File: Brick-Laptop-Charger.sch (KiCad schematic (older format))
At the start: 46 parts, among them P1 TST, P10 Power Out, P2 TST, P3 TST, P4 TST, P5 TST, P6 TST, P7 TST, P8 Battery 1, P9 Battery 2, Q1 MOS_N, Q2 MOS_N, U1 LM5117*PM*

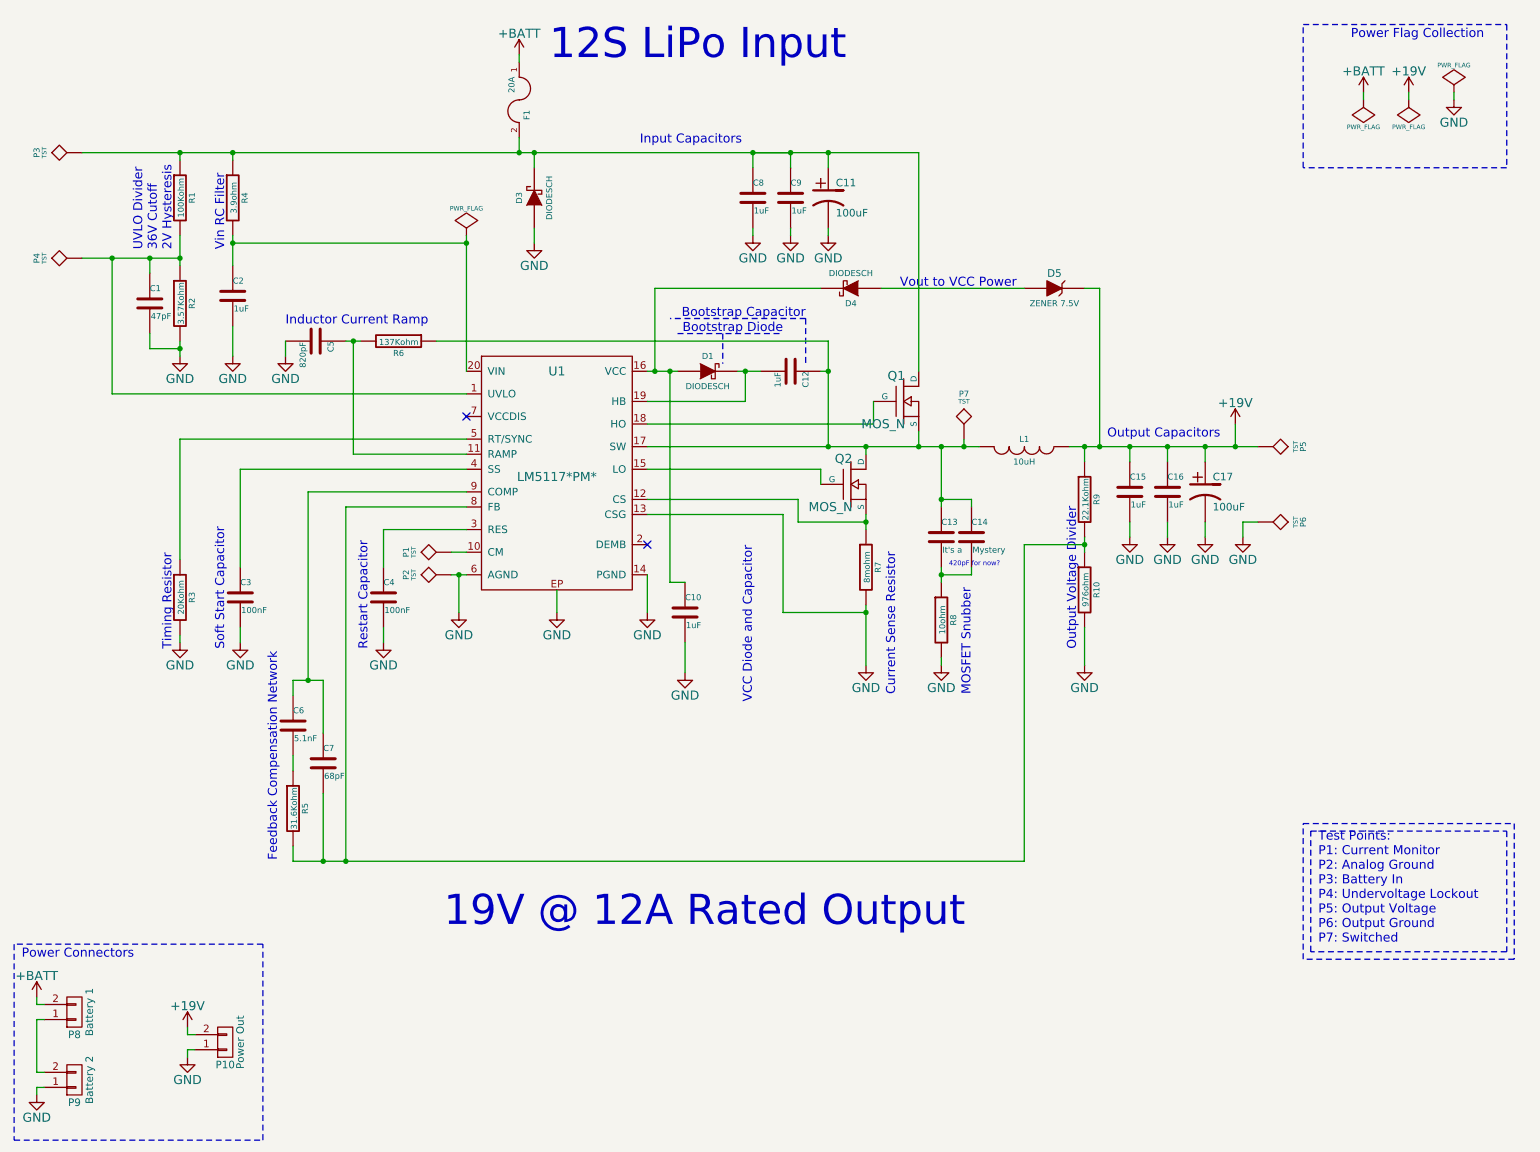
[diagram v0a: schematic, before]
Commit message: Separated analog and power grounds.  Most of power current now flows through a separate path from analog circuitry (see exposed trace on bottom of PCB).  Reduced capacitive coupling between ground planes and MOSFET switches.  Smoothed copper pours.  Added power in LED.
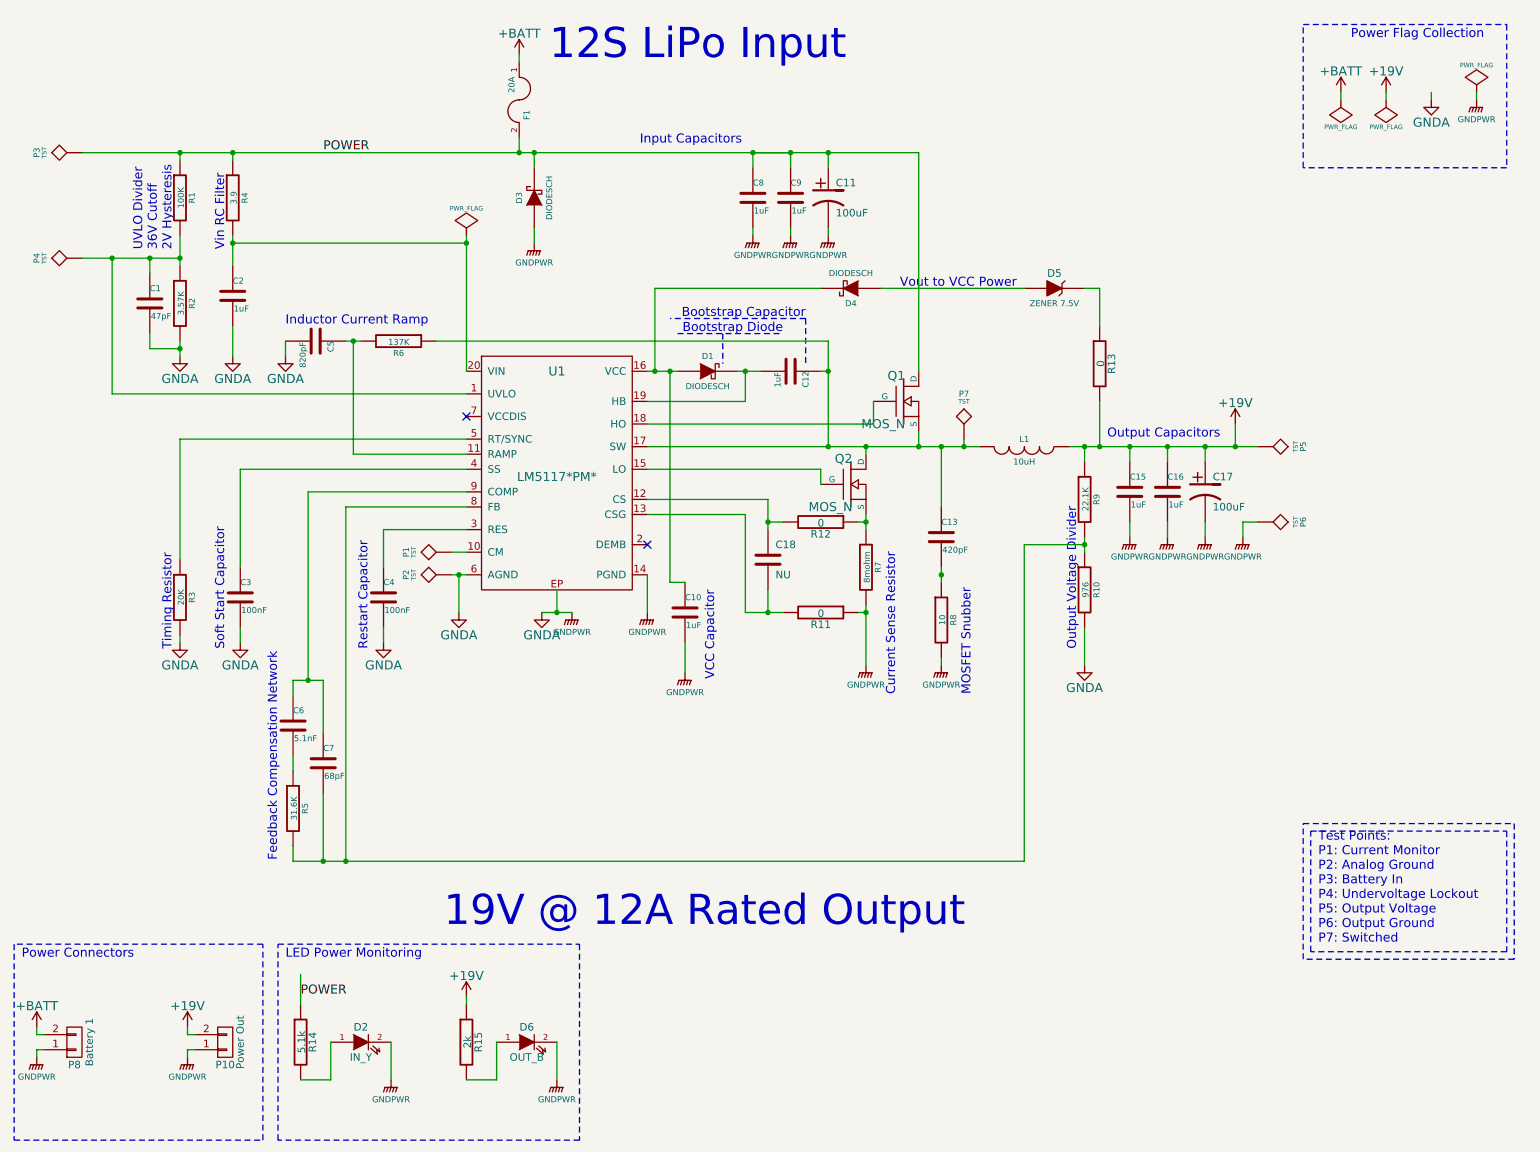
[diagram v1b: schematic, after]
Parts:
- removed C14: Mystery, Discret:C1, symbol C
- removed P9: Battery 2, This:BIG_CONN, symbol CONN_01X02
- added C18: NU, Capacitors_SMD:C_0805, symbol C
- added D2: IN_Y, LEDs:LED-0805, symbol LED
- added D6: OUT_B, LEDs:LED-0805, symbol LED
- added R11, R12, R13: 0, Resistors_SMD:R_0805, symbol R
- added R14: 5.1k, Resistors_SMD:R_0805, symbol R
- added R15: 2k, Resistors_SMD:R_0805, symbol R
- C13: value It's a -> 420pF
- R1: value 100Kohm -> 100K
- R10: value 976ohm -> 976
- R2: value 3.57Kohm -> 3.57K
- R3: value 20Kohm -> 20K
- R4: value 3.9ohm -> 3.9
- R5: value 31.6Kohm -> 31.6K
- R6: value 137Kohm -> 137K
- R8: value 10ohm -> 10
- R9: value 22.1Kohm -> 22.1K
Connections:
- net +19V: now also R13.2, R15.1; no longer D5.2 (K)
- net at Q2.S, R7.1: now also R12.1; no longer U1.12 (CS)
- net POWER: now reaches C11.1, C8.1, C9.1, D3.2 (K), F1.2, P3.1, Q1.D, R1.1, R4.1
- net POWER: now also R14.1
- net GNDA: now reaches P8.1 (P1)
- net GNDA: now also C1.2, C10.2, C11.2, C15.2, C16.2, C17.2, C2.2, C3.2, C4.2, C5.2, C8.2, C9.2, D3.1 (A), P10.1 (P1), P2.1, P6.1, R10.2, R2.2, R3.2, R7.2, R8.2, U1.14 (PGND), U1.6 (AGND), U1.EP, D2.2 (K), D6.2 (K), R11.1
- removed net GND: C1.2, C10.2, C11.2, C15.2, C16.2, C17.2, C2.2, C3.2, C4.2, C5.2, C8.2, C9.2, D3.1 (A), P10.1 (P1), P2.1, P6.1, R10.2, R2.2, R3.2, R7.2, R8.2, U1.13 (CSG), U1.14 (PGND), U1.6 (AGND), U1.EP
- new net: C18.1, R12.2, U1.12 (CS)
- new net: C18.2, R11.2, U1.13 (CSG)
- new net: D5.2 (K), R13.1
- new net: D2.1 (A), R14.2
- new net: D6.1 (A), R15.2
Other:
- note added: "LED Power Monitoring"
- note added: "VCC Capacitor"
- note removed: "420pF for now?"
- note removed: "VCC Diode and Capacitor"
- moved on the sheet: P8

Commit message: Moved files, removed backup files, added important notes about inductor selection, added images
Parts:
- removed D2: IN_Y, LEDs:LED-0805, symbol LED
- removed R14: 5.1k, Resistors_SMD:R_0805, symbol R
- C1, C10, C12, C13, C15, C16, C18, C2, C3, C4, C5, C6, C7, C8, C9: symbol C -> C-RESCUE-Brick-Laptop-Charger
- C11, C17: symbol CP1 -> CP1-RESCUE-Brick-Laptop-Charger
- D5: symbol ZENER -> ZENER-RESCUE-Brick-Laptop-Charger
- D6: symbol LED -> LED-RESCUE-Brick-Laptop-Charger
- R1, R10, R11, R12, R13, R15, R2, R3, R4, R5, R6, R7, R8, R9: symbol R -> R-RESCUE-Brick-Laptop-Charger
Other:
- moved on the sheet: D6, R15
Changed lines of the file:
@@
 EESchema Schematic File Version 2
+LIBS:Brick-Laptop-Charger-rescue
 LIBS:+19v
 LIBS:power
@@
 LIBS:memory
 LIBS:xilinx
-LIBS:special
 LIBS:microcontrollers
 LIBS:dsp
@@
 Sheet 1 1
 Title "Yellow Brick Laptop Charger Schematic"
-Date "Tue 10 Feb 2015"
-Rev "C"
+Date "2015-08-12"
+Rev "D"
 Comp "IEEE UCR, UCR UAS"
 Comment1 "By: Brandon (blu006@ucr.edu)"
@@
 $EndComp
 $Comp
-L C C15
+L C-RESCUE-Brick-Laptop-Charger C15
 U 1 1 54992FF6
 P 7950 3650
@@
 $EndComp
 $Comp
-L C C16
+L C-RESCUE-Brick-Laptop-Charger C16
 U 1 1 54993133
 P 8200 3650
@@
 $EndComp
 $Comp
-L CP1 C17
+L CP1-RESCUE-Brick-Laptop-Charger C17
 U 1 1 54993168
 P 8450 3650
@@
 $EndComp
 $Comp
-L C C12
+L C-RESCUE-Brick-Laptop-Charger C12
 U 1 1 54993759
 P 5700 2850
@@
 $EndComp
 $Comp
-L C C10
+L C-RESCUE-Brick-Laptop-Charger C10
 U 1 1 54993858
 P 5000 4450
@@
 $EndComp
 $Comp
-L R R8
+L R-RESCUE-Brick-Laptop-Charger R8
 U 1 1 54993C5B
 P 6700 4500
@@
 $EndComp
 $Comp
-L R R7
+L R-RESCUE-Brick-Laptop-Charger R7
 U 1 1 54993FF3
 P 6200 4150
@@
 $EndComp
 $Comp
-L C C5
+L C-RESCUE-Brick-Laptop-Charger C5
 U 1 1 54995580
 P 2550 2650
@@
 $EndComp
 $Comp
-L R R6
+L R-RESCUE-Brick-Laptop-Charger R6
 U 1 1 549959D5
 P 3100 2650
@@
 $EndComp
 $Comp
-L R R3
+L R-RESCUE-Brick-Laptop-Charger R3
 U 1 1 54996578
 P 1650 4350
@@
 $EndComp
 $Comp
-L R R1
+L R-RESCUE-Brick-Laptop-Charger R1
 U 1 1 5499683E
 P 1650 1700
@@
 $EndComp
 $Comp
-L R R2
+L R-RESCUE-Brick-Laptop-Charger R2
 U 1 1 549969E4
 P 1650 2400
@@
 $EndComp
 $Comp
-L R R4
+L R-RESCUE-Brick-Laptop-Charger R4
 U 1 1 54996D8E
 P 2000 1700
@@
 $EndComp
 $Comp
-L C C2
+L C-RESCUE-Brick-Laptop-Charger C2
 U 1 1 54996DF9
 P 2000 2350
@@
 $EndComp
 $Comp
-L C C1
+L C-RESCUE-Brick-Laptop-Charger C1
 U 1 1 54997D5E
 P 1450 2400
@@
 $EndComp
 $Comp
-L C C3
+L C-RESCUE-Brick-Laptop-Charger C3
 U 1 1 54998944
 P 2050 4350
@@
 Current Sense Resistor
 $Comp
-L C C4
+L C-RESCUE-Brick-Laptop-Charger C4
 U 1 1 54999F5C
 P 3000 4350
@@
 $EndComp
 $Comp
-L R R9
+L R-RESCUE-Brick-Laptop-Charger R9
 U 1 1 5499B371
 P 7650 3700
@@
 $EndComp
 $Comp
-L R R10
+L R-RESCUE-Brick-Laptop-Charger R10
 U 1 1 5499B44E
 P 7650 4300
@@
 Output Voltage Divider
 $Comp
-L C C7
+L C-RESCUE-Brick-Laptop-Charger C7
 U 1 1 5499CDE4
 P 2600 5450
@@
 $EndComp
 $Comp
-L C C6
+L C-RESCUE-Brick-Laptop-Charger C6
 U 1 1 5499CE97
 P 2400 5200
@@
 $EndComp
 $Comp
-L R R5
+L R-RESCUE-Brick-Laptop-Charger R5
 U 1 1 5499CEEA
 P 2400 5750
@@
 VCC Capacitor
 $Comp
-L C C8
+L C-RESCUE-Brick-Laptop-Charger C8
 U 1 1 549A0DE6
 P 5450 1700
@@
 $EndComp
 $Comp
-L C C9
+L C-RESCUE-Brick-Laptop-Charger C9
 U 1 1 549A0DEC
 P 5700 1700
@@
 $EndComp
 $Comp
-L CP1 C11
+L CP1-RESCUE-Brick-Laptop-Charger C11
 U 1 1 549A0DF2
 P 5950 1700
@@
 Wire Wire Line
 	1000 1400 6550 1400
-Connection ~ 6700 4200
 Wire Wire Line
 	2400 6000 2400 6100
@@
 	4000 2000 4000 1900
 $Comp
-L ZENER D5
+L ZENER-RESCUE-Brick-Laptop-Charger D5
 U 1 1 549C5A81
 P 7450 2300
@@
 	700  7350 700  7400
 $Comp
-L R R11
+L R-RESCUE-Brick-Laptop-Charger R11
 U 1 1 54D43E7E
 P 5900 4450
@@
 $EndComp
 $Comp
-L R R12
+L R-RESCUE-Brick-Laptop-Charger R12
 U 1 1 54D46259
 P 5900 3850
@@
 	6150 3850 6200 3850
 $Comp
-L R R13
+L R-RESCUE-Brick-Laptop-Charger R13
 U 1 1 54D47065
 P 7750 2800
@@
 	7750 2300 7750 2550
 $Comp
-L C C18
+L C-RESCUE-Brick-Laptop-Charger C18
 U 1 1 54D47CFC
 P 5550 4100
@@
 	5550 3850 5650 3850
 $Comp
-L C C13
+L C-RESCUE-Brick-Laptop-Charger C13
 U 1 1 54993BF7
 P 6700 3950
@@
 L +19V #PWR037
 U 1 1 54D81731
-P 3550 7000
-F 0 "#PWR037" H 3550 6850 60  0001 C CNN
-F 1 "+19V" H 3550 7140 60  0000 C CNN
-F 2 "" H 3550 7000 60  0000 C CNN
-F 3 "" H 3550 7000 60  0000 C CNN
-	1    3550 7000
-	1    0    0    -1
-$EndComp
-$Comp
-L R R14
-U 1 1 54D81895
-P 2450 7300
-F 0 "R14" V 2530 7300 50  0000 C CNN
-F 1 "5.1k" V 2457 7301 50  0000 C CNN
-F 2 "Resistors_SMD:R_0805" V 2380 7300 30  0001 C CNN
-F 3 "" H 2450 7300 30  0000 C CNN
-	1    2450 7300
-	1    0    0    -1
-$EndComp
-$Comp
-L R R15
+P 3000 7000
+F 0 "#PWR037" H 3000 6850 60  0001 C CNN
+F 1 "+19V" H 3000 7140 60  0000 C CNN
+F 2 "" H 3000 7000 60  0000 C CNN
+F 3 "" H 3000 7000 60  0000 C CNN
+	1    3000 7000
+	1    0    0    -1
+$EndComp
+$Comp
+L R-RESCUE-Brick-Laptop-Charger R15
 U 1 1 54D818CE
-P 3550 7300
-F 0 "R15" V 3630 7300 50  0000 C CNN
-F 1 "2k" V 3557 7301 50  0000 C CNN
-F 2 "Resistors_SMD:R_0805" V 3480 7300 30  0001 C CNN
-F 3 "" H 3550 7300 30  0000 C CNN
-	1    3550 7300
-	1    0    0    -1
-$EndComp
-$Comp
-L LED D2
-U 1 1 54D81CD3
-P 2850 7300
-F 0 "D2" H 2850 7400 50  0000 C CNN
-F 1 "IN_Y" H 2850 7200 50  0000 C CNN
-F 2 "LEDs:LED-0805" H 2850 7300 60  0001 C CNN
-F 3 "" H 2850 7300 60  0000 C CNN
-	1    2850 7300
-	1    0    0    -1
-$EndComp
-$Comp
-L GNDPWR #PWR038
-U 1 1 54D81E87
-P 3050 7550
-F 0 "#PWR038" H 3050 7350 40  0001 C CNN
-F 1 "GNDPWR" H 3050 7420 40  0000 C CNN
-F 2 "" H 3050 7500 60  0000 C CNN
-F 3 "" H 3050 7500 60  0000 C CNN
-	1    3050 7550
-	1    0    0    -1
-$EndComp
-$Comp
-L LED D6
+P 3000 7300
+F 0 "R15" V 3080 7300 50  0000 C CNN
+F 1 "2k" V 3007 7301 50  0000 C CNN
+F 2 "Resistors_SMD:R_0805" V 2930 7300 30  0001 C CNN
+F 3 "" H 3000 7300 30  0000 C CNN
+	1    3000 7300
+	1    0    0    -1
+$EndComp
+$Comp
+L LED-RESCUE-Brick-Laptop-Charger D6
 U 1 1 54D8215B
-P 3950 7300
-F 0 "D6" H 3950 7400 50  0000 C CNN
-F 1 "OUT_B" H 3950 7200 50  0000 C CNN
-F 2 "LEDs:LED-0805" H 3950 7300 60  0001 C CNN
-F 3 "" H 3950 7300 60  0000 C CNN
-	1    3950 7300
+P 3400 7300
+F 0 "D6" H 3400 7400 50  0000 C CNN
+F 1 "OUT_B" H 3400 7200 50  0000 C CNN
+F 2 "LEDs:LED-0805" H 3400 7300 60  0001 C CNN
+F 3 "" H 3400 7300 60  0000 C CNN
+	1    3400 7300
 	1    0    0    -1
 $EndComp
@@
 L GNDPWR #PWR039
 U 1 1 54D82161
-P 4150 7550
-F 0 "#PWR039" H 4150 7350 40  0001 C CNN
-F 1 "GNDPWR" H 4150 7420 40  0000 C CNN
-F 2 "" H 4150 7500 60  0000 C CNN
-F 3 "" H 4150 7500 60  0000 C CNN
-	1    4150 7550
-	1    0    0    -1
-$EndComp
-Wire Wire Line
-	2450 7550 2650 7550
-Wire Wire Line
-	2650 7550 2650 7300
-Wire Wire Line
-	3050 7300 3050 7550
-Wire Wire Line
-	3550 7550 3750 7550
-Wire Wire Line
-	3750 7550 3750 7300
-Wire Wire Line
-	4150 7300 4150 7550
-Wire Wire Line
-	2450 6850 2450 7050
-Wire Wire Line
-	3550 7050 3550 7000
+P 3600 7550
+F 0 "#PWR039" H 3600 7350 40  0001 C CNN
+F 1 "GNDPWR" H 3600 7420 40  0000 C CNN
+F 2 "" H 3600 7500 60  0000 C CNN
+F 3 "" H 3600 7500 60  0000 C CNN
+	1    3600 7550
+	1    0    0    -1
+$EndComp
+Wire Wire Line
+	3000 7550 3200 7550
+Wire Wire Line
+	3200 7550 3200 7300
+Wire Wire Line
+	3600 7300 3600 7550
+Wire Wire Line
+	3000 7050 3000 7000
 Wire Notes Line
 	2300 6650 4300 6650
@@
 Text Label 2600 1400 0    60   ~ 0
 POWER
-Text Label 2450 7000 0    60   ~ 0
-POWER
-Wire Wire Line
+Wire Wire Line
